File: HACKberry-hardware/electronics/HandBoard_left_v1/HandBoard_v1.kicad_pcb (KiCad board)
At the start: 2 copper layers, 60.8 x 54.8 mm, 12 parts, among them CON1 BARREL_JACK, SW1:MAX1 SW_PUSH_SKRGAQD010, SW2:MIN1 SW_PUSH_SKRGAQD010, SW3:Thumb1 SW_PUSH_SKRGAQD010, SW4:Middle1 SW_PUSH_SKRGAQD010, SW5 SWITCH_SS-12SDP2, U1 3-CONDUCTOR_MINIATUIRE_JACK_M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, U2 Arduino_Micro, U3 Seed_Studio_Adjustable_DC/DC_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, U4 Servo_Motor_S03N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

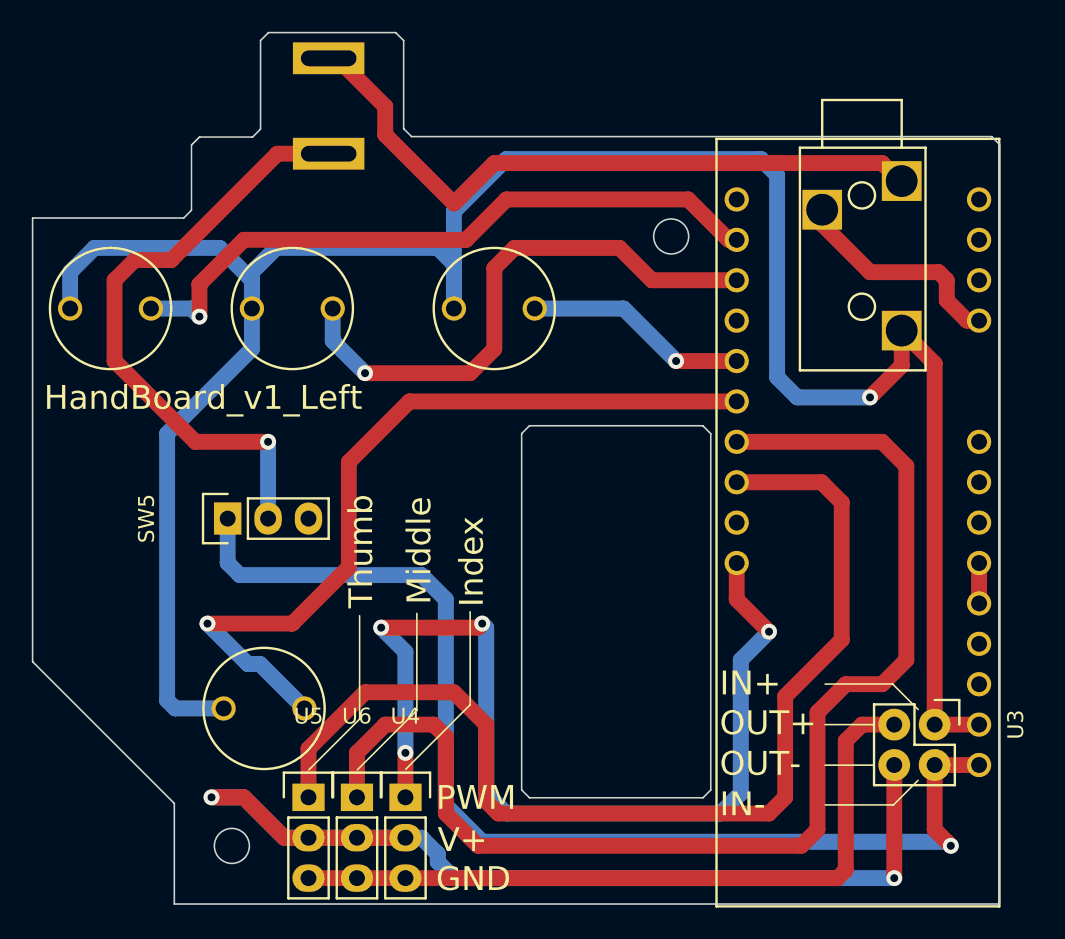
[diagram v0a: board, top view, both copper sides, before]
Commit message: MJ179PHを追加したがkicadさん馬鹿なので数字が一致してるかどうかの判定ができずにschとbrdの整合を取れないらしい
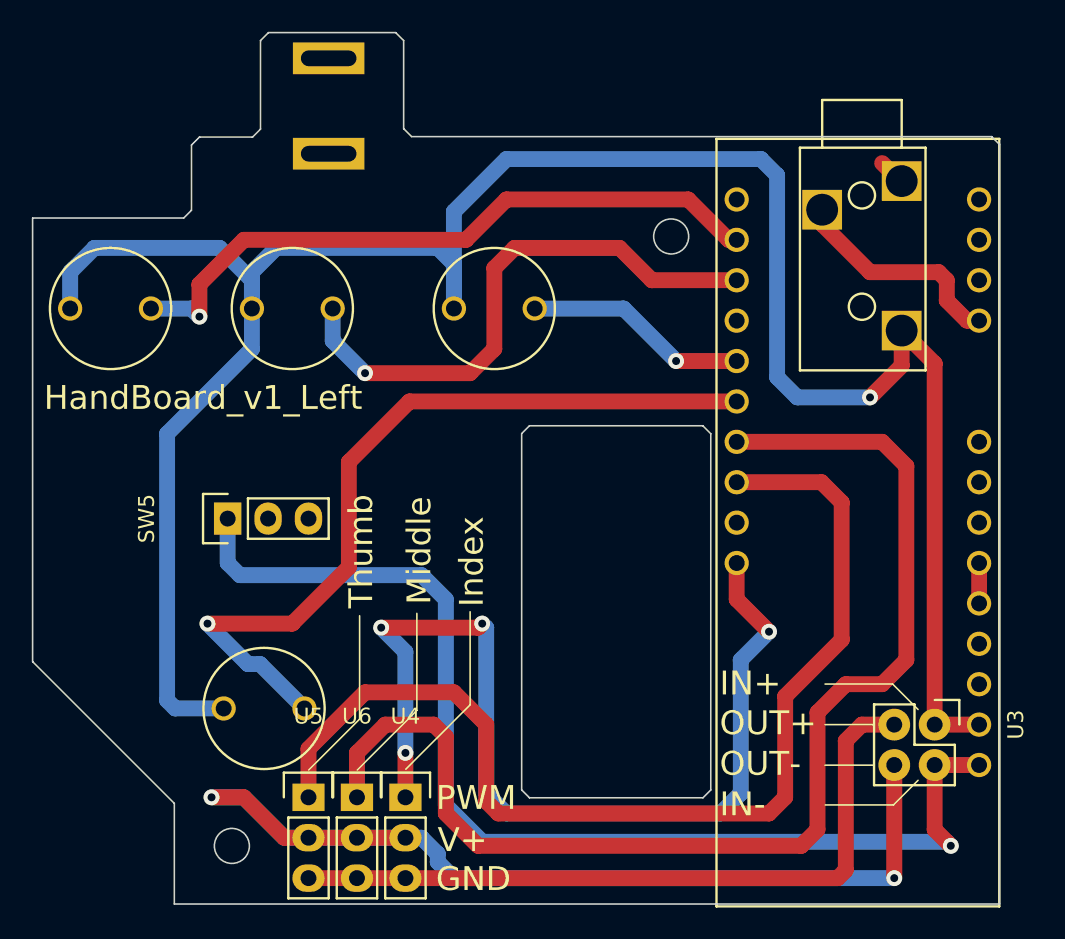
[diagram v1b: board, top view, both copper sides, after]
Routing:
- net Net-(U1-Pad2): track 42.4 -> 1.70 mm
- net Net-(CON1-Pad1): track 38.4 -> 0.00 mm, vias 1 -> 0
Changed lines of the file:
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@@
     (links 23)
     (no_connects 1)
-    (area 95.3061 68.711552 159.4021 154.678413)
+    (area 96.561099 85.319599 157.461101 140.209601)
     (thickness 1.6)
     (drawings 55)
-    (tracks 181)
+    (tracks 163)
     (zones 0)
     (modules 12)
@@
   (gr_circle (center 136.7607 98.1868) (end 137.8607 98.1868) (layer Edge.Cuts) (width 0.1))
   (gr_circle (center 109.1407 136.5068) (end 110.2407 136.5068) (layer Edge.Cuts) (width 0.1))
-  (segment (start 115.2271 92.9856) (end 112.0051 92.9856) (width 1) (layer F.Cu) (net 1))
-  (segment (start 111.4171 111.0996) (end 111.4171 115.9256) (width 1) (layer B.Cu) (net 1))
-  (via (at 111.4171 111.0996) (size 1) (drill 0.5) (layers F.Cu B.Cu) (net 1))
-  (segment (start 106.8451 111.0996) (end 111.4171 111.0996) (width 1) (layer F.Cu) (net 1))
-  (segment (start 101.7651 106.0196) (end 106.8451 111.0996) (width 1) (layer F.Cu) (net 1))
-  (segment (start 101.7651 100.9396) (end 101.7651 106.0196) (width 1) (layer F.Cu) (net 1))
-  (segment (start 103.0351 99.6696) (end 101.7651 100.9396) (width 1) (layer F.Cu) (net 1))
-  (segment (start 105.3211 99.6696) (end 103.0351 99.6696) (width 1) (layer F.Cu) (net 1))
-  (segment (start 112.0051 92.9856) (end 105.3211 99.6696) (width 1) (layer F.Cu) (net 1))
   (segment (start 153.3271 131.4196) (end 153.3271 135.4836) (width 1) (layer F.Cu) (net 2))
   (segment (start 108.8771 118.7196) (end 108.8771 115.9256) (width 1) (layer B.Cu) (net 2))
@@
   (segment (start 146.2551 96.5056) (end 146.2551 97.1696) (width 1) (layer F.Cu) (net 4))
   (segment (start 146.2551 96.5056) (end 146.3531 96.5056) (width 1) (layer F.Cu) (net 4))
-  (segment (start 115.2271 86.9856) (end 115.7511 86.9856) (width 1) (layer F.Cu) (net 5))
-  (segment (start 115.7511 86.9856) (end 118.7831 90.0176) (width 1) (layer F.Cu) (net 5))
-  (segment (start 118.7831 90.0176) (end 118.7831 91.7956) (width 1) (layer F.Cu) (net 5))
-  (segment (start 118.7831 91.7956) (end 123.1011 96.1136) (width 1) (layer F.Cu) (net 5))
   (segment (start 151.2551 94.7056) (end 151.1571 94.7056) (width 1) (layer F.Cu) (net 5))
   (segment (start 151.1571 94.7056) (end 150.0251 93.5736) (width 1) (layer F.Cu) (net 5))
-  (segment (start 150.0251 93.5736) (end 143.4211 93.5736) (width 1) (layer F.Cu) (net 5))
-  (segment (start 143.4211 93.5736) (end 142.1511 93.5736) (width 1) (layer F.Cu) (net 5))
-  (segment (start 142.1511 93.5736) (end 141.8971 93.5736) (width 1) (layer F.Cu) (net 5))
-  (segment (start 141.8971 93.5736) (end 125.6411 93.5736) (width 1) (layer F.Cu) (net 5))
-  (segment (start 125.6411 93.5736) (end 123.1011 96.1136) (width 1) (layer F.Cu) (net 5))
   (segment (start 156.1211 123.7996) (end 156.1211 123.7896) (width 0.5) (layer F.Cu) (net 6) (status 30))
   (segment (start 156.1211 121.2596) (end 156.1211 118.7196) (width 1) (layer F.Cu) (net 7))
